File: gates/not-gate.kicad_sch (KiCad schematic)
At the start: 5 parts, among them Q7 NPN, Q8 NPN

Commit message: Schematic for register
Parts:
- removed Q7, Q8: NPN, symbol Simulation_SPICE:NPN
- removed R12, R13: 10k, Resistor_SMD:R_0201_0603Metric, symbol Device:R
- removed R14: 4.7k, Resistor_SMD:R_0201_0603Metric, symbol Device:R
- added Q1: NPN, symbol Simulation_SPICE:NPN
- added R1: 10k, symbol Device:R
- added R2: 4.7k, symbol Device:R
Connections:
- net +5V: now also R2.2
- net A: now also R1.1
- net GND: now also Q1.3 (E)
- net OUTPUT: now also Q1.1 (C), R2.1
- new net: Q1.2 (B), R1.2

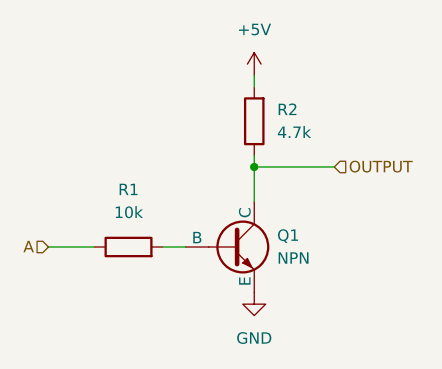
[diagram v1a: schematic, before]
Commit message: Schematic of control-unit
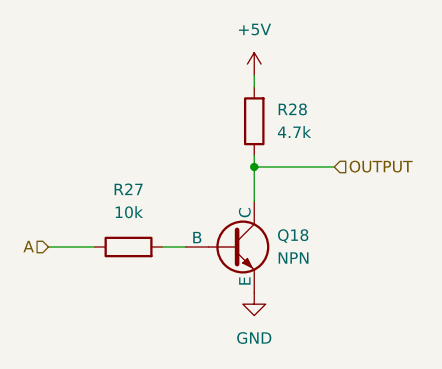
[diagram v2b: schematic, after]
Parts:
- renumbered Q1 to Q18, R1 to R27, R2 to R28
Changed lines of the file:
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@@
 		(dnp no)
 		(fields_autoplaced yes)
-		(property "Reference" "#PWR05"
+		(property "Reference" "#PWR027"
 			(at 87.63 55.88 0)
 			(effects
@@
 		)
 		(instances
-			(project "register"
-				(path "/176ebc34-d92d-46b0-a9f1-4fb76aa55196/1641c1b9-e3d9-452a-a206-0a4a18cb7a68/6e38e628-9b38-49db-b4e0-13318949e362"
-					(reference "#PWR019")
-					(unit 1)
-				)
-				(path "/176ebc34-d92d-46b0-a9f1-4fb76aa55196/2b210005-c9ef-43dd-bd20-4304cf65b93c/6e38e628-9b38-49db-b4e0-13318949e362"
-					(reference "#PWR05")
-					(unit 1)
-				)
-				(path "/176ebc34-d92d-46b0-a9f1-4fb76aa55196/475a755d-c11d-42bc-b5a5-c2bbb617acf6/6e38e628-9b38-49db-b4e0-13318949e362"
-					(reference "#PWR047")
-					(unit 1)
-				)
-				(path "/176ebc34-d92d-46b0-a9f1-4fb76aa55196/510c109f-9f77-4fcd-9065-7421496291db/6e38e628-9b38-49db-b4e0-13318949e362"
-					(reference "#PWR033")
+			(project "control-unit"
+				(path "/1cf3a7ee-ec47-45b6-b515-1840d726ab8f/020249bf-5e28-4526-a135-e7e504fcd315"
+					(reference "#PWR?")
+					(unit 1)
+				)
+				(path "/1cf3a7ee-ec47-45b6-b515-1840d726ab8f/0384bfed-f155-4b67-acfd-5caa02b59c9d"
+					(reference "#PWR027")
+					(unit 1)
+				)
+				(path "/1cf3a7ee-ec47-45b6-b515-1840d726ab8f/32697942-fb33-4fba-8e0d-2ff095b080bf"
+					(reference "#PWR017")
+					(unit 1)
+				)
+				(path "/1cf3a7ee-ec47-45b6-b515-1840d726ab8f/80b2507e-0011-4117-8a6b-d09ffa023d4d"
+					(reference "#PWR039")
+					(unit 1)
+				)
+				(path "/1cf3a7ee-ec47-45b6-b515-1840d726ab8f/b2ec3573-bf15-4e1d-8a02-9a033baafe0c"
+					(reference "#PWR021")
+					(unit 1)
+				)
+				(path "/1cf3a7ee-ec47-45b6-b515-1840d726ab8f/b421555f-23f8-4bc1-97f9-21732f6fe247"
+					(reference "#PWR025")
 					(unit 1)
 				)
@@
 		(dnp no)
 		(fields_autoplaced yes)
-		(property "Reference" "R1"
+		(property "Reference" "R27"
 			(at 73.66 64.77 90)
 			(effects
@@
 		)
 		(instances
-			(project "register"
-				(path "/176ebc34-d92d-46b0-a9f1-4fb76aa55196/1641c1b9-e3d9-452a-a206-0a4a18cb7a68/6e38e628-9b38-49db-b4e0-13318949e362"
+			(project "control-unit"
+				(path "/1cf3a7ee-ec47-45b6-b515-1840d726ab8f/020249bf-5e28-4526-a135-e7e504fcd315"
+					(reference "R?")
+					(unit 1)
+				)
+				(path "/1cf3a7ee-ec47-45b6-b515-1840d726ab8f/0384bfed-f155-4b67-acfd-5caa02b59c9d"
+					(reference "R27")
+					(unit 1)
+				)
+				(path "/1cf3a7ee-ec47-45b6-b515-1840d726ab8f/32697942-fb33-4fba-8e0d-2ff095b080bf"
+					(reference "R23")
+					(unit 1)
+				)
+				(path "/1cf3a7ee-ec47-45b6-b515-1840d726ab8f/80b2507e-0011-4117-8a6b-d09ffa023d4d"
+					(reference "R37")
+					(unit 1)
+				)
+				(path "/1cf3a7ee-ec47-45b6-b515-1840d726ab8f/b2ec3573-bf15-4e1d-8a02-9a033baafe0c"
 					(reference "R17")
 					(unit 1)
 				)
-				(path "/176ebc34-d92d-46b0-a9f1-4fb76aa55196/2b210005-c9ef-43dd-bd20-4304cf65b93c/6e38e628-9b38-49db-b4e0-13318949e362"
-					(reference "R1")
-					(unit 1)
-				)
-				(path "/176ebc34-d92d-46b0-a9f1-4fb76aa55196/475a755d-c11d-42bc-b5a5-c2bbb617acf6/6e38e628-9b38-49db-b4e0-13318949e362"
-					(reference "R49")
-					(unit 1)
-				)
-				(path "/176ebc34-d92d-46b0-a9f1-4fb76aa55196/510c109f-9f77-4fcd-9065-7421496291db/6e38e628-9b38-49db-b4e0-13318949e362"
-					(reference "R33")
+				(path "/1cf3a7ee-ec47-45b6-b515-1840d726ab8f/b421555f-23f8-4bc1-97f9-21732f6fe247"
+					(reference "R25")
 					(unit 1)
 				)
@@
 		(dnp no)
 		(fields_autoplaced yes)
-		(property "Reference" "R2"
+		(property "Reference" "R28"
 			(at 90.17 55.8799 0)
 			(effects
@@
 		)
 		(instances
-			(project "register"
-				(path "/176ebc34-d92d-46b0-a9f1-4fb76aa55196/1641c1b9-e3d9-452a-a206-0a4a18cb7a68/6e38e628-9b38-49db-b4e0-13318949e362"
+			(project "control-unit"
+				(path "/1cf3a7ee-ec47-45b6-b515-1840d726ab8f/020249bf-5e28-4526-a135-e7e504fcd315"
+					(reference "R?")
+					(unit 1)
+				)
+				(path "/1cf3a7ee-ec47-45b6-b515-1840d726ab8f/0384bfed-f155-4b67-acfd-5caa02b59c9d"
+					(reference "R28")
+					(unit 1)
+				)
+				(path "/1cf3a7ee-ec47-45b6-b515-1840d726ab8f/32697942-fb33-4fba-8e0d-2ff095b080bf"
+					(reference "R24")
+					(unit 1)
+				)
+				(path "/1cf3a7ee-ec47-45b6-b515-1840d726ab8f/80b2507e-0011-4117-8a6b-d09ffa023d4d"
+					(reference "R38")
+					(unit 1)
+				)
+				(path "/1cf3a7ee-ec47-45b6-b515-1840d726ab8f/b2ec3573-bf15-4e1d-8a02-9a033baafe0c"
 					(reference "R18")
 					(unit 1)
 				)
-				(path "/176ebc34-d92d-46b0-a9f1-4fb76aa55196/2b210005-c9ef-43dd-bd20-4304cf65b93c/6e38e628-9b38-49db-b4e0-13318949e362"
-					(reference "R2")
-					(unit 1)
-				)
-				(path "/176ebc34-d92d-46b0-a9f1-4fb76aa55196/475a755d-c11d-42bc-b5a5-c2bbb617acf6/6e38e628-9b38-49db-b4e0-13318949e362"
-					(reference "R50")
-					(unit 1)
-				)
-				(path "/176ebc34-d92d-46b0-a9f1-4fb76aa55196/510c109f-9f77-4fcd-9065-7421496291db/6e38e628-9b38-49db-b4e0-13318949e362"
-					(reference "R34")
+				(path "/1cf3a7ee-ec47-45b6-b515-1840d726ab8f/b421555f-23f8-4bc1-97f9-21732f6fe247"
+					(reference "R26")
 					(unit 1)
 				)
@@
 		(dnp no)
 		(fields_autoplaced yes)
-		(property "Reference" "#PWR06"
+		(property "Reference" "#PWR028"
 			(at 87.63 82.55 0)
 			(effects
@@
 		)
 		(instances
-			(project "register"
-				(path "/176ebc34-d92d-46b0-a9f1-4fb76aa55196/1641c1b9-e3d9-452a-a206-0a4a18cb7a68/6e38e628-9b38-49db-b4e0-13318949e362"
-					(reference "#PWR020")
-					(unit 1)
-				)
-				(path "/176ebc34-d92d-46b0-a9f1-4fb76aa55196/2b210005-c9ef-43dd-bd20-4304cf65b93c/6e38e628-9b38-49db-b4e0-13318949e362"
-					(reference "#PWR06")
-					(unit 1)
-				)
-				(path "/176ebc34-d92d-46b0-a9f1-4fb76aa55196/475a755d-c11d-42bc-b5a5-c2bbb617acf6/6e38e628-9b38-49db-b4e0-13318949e362"
-					(reference "#PWR048")
-					(unit 1)
-				)
-				(path "/176ebc34-d92d-46b0-a9f1-4fb76aa55196/510c109f-9f77-4fcd-9065-7421496291db/6e38e628-9b38-49db-b4e0-13318949e362"
-					(reference "#PWR034")
+			(project "control-unit"
+				(path "/1cf3a7ee-ec47-45b6-b515-1840d726ab8f/020249bf-5e28-4526-a135-e7e504fcd315"
+					(reference "#PWR?")
+					(unit 1)
+				)
+				(path "/1cf3a7ee-ec47-45b6-b515-1840d726ab8f/0384bfed-f155-4b67-acfd-5caa02b59c9d"
+					(reference "#PWR028")
+					(unit 1)
+				)
+				(path "/1cf3a7ee-ec47-45b6-b515-1840d726ab8f/32697942-fb33-4fba-8e0d-2ff095b080bf"
+					(reference "#PWR018")
+					(unit 1)
+				)
+				(path "/1cf3a7ee-ec47-45b6-b515-1840d726ab8f/80b2507e-0011-4117-8a6b-d09ffa023d4d"
+					(reference "#PWR040")
+					(unit 1)
+				)
+				(path "/1cf3a7ee-ec47-45b6-b515-1840d726ab8f/b2ec3573-bf15-4e1d-8a02-9a033baafe0c"
+					(reference "#PWR022")
+					(unit 1)
+				)
+				(path "/1cf3a7ee-ec47-45b6-b515-1840d726ab8f/b421555f-23f8-4bc1-97f9-21732f6fe247"
+					(reference "#PWR026")
 					(unit 1)
 				)
@@
 		(dnp no)
 		(fields_autoplaced yes)
-		(property "Reference" "Q1"
+		(property "Reference" "Q18"
 			(at 90.17 69.8499 0)
 			(effects
@@
 		)
 		(instances
-			(project "register"
-				(path "/176ebc34-d92d-46b0-a9f1-4fb76aa55196/1641c1b9-e3d9-452a-a206-0a4a18cb7a68/6e38e628-9b38-49db-b4e0-13318949e362"
-					(reference "Q12")
-					(unit 1)
-				)
-				(path "/176ebc34-d92d-46b0-a9f1-4fb76aa55196/2b210005-c9ef-43dd-bd20-4304cf65b93c/6e38e628-9b38-49db-b4e0-13318949e362"
-					(reference "Q1")
-					(unit 1)
-				)
-				(path "/176ebc34-d92d-46b0-a9f1-4fb76aa55196/475a755d-c11d-42bc-b5a5-c2bbb617acf6/6e38e628-9b38-49db-b4e0-13318949e362"
-					(reference "Q34")
-					(unit 1)
-				)
-				(path "/176ebc34-d92d-46b0-a9f1-4fb76aa55196/510c109f-9f77-4fcd-9065-7421496291db/6e38e628-9b38-49db-b4e0-13318949e362"
-					(reference "Q23")
-					(unit 1)
-				)
+			(project "control-unit"
+				(path "/1cf3a7ee-ec47-45b6-b515-1840d726ab8f/020249bf-5e28-4526-a135-e7e504fcd315"
+					(reference "Q?")
+					(unit 1)
+				)
+				(path "/1cf3a7ee-ec47-45b6-b515-1840d726ab8f/0384bfed-f155-4b67-acfd-5caa02b59c9d"
+					(reference "Q18")
+					(unit 1)
+				)
+				(path "/1cf3a7ee-ec47-45b6-b515-1840d726ab8f/32697942-fb33-4fba-8e0d-2ff095b080bf"
+					(reference "Q16")
+					(unit 1)
+				)
+				(path "/1cf3a7ee-ec47-45b6-b515-1840d726ab8f/80b2507e-0011-4117-8a6b-d09ffa023d4d"
+					(reference "Q26")
+					(unit 1)
+				)
+				(path "/1cf3a7ee-ec47-45b6-b515-1840d726ab8f/b2ec3573-bf15-4e1d-8a02-9a033baafe0c"
+					(reference "Q13")
+					(unit 1)
+				)
+				(path "/1cf3a7ee-ec47-45b6-b515-1840d726ab8f/b421555f-23f8-4bc1-97f9-21732f6fe247"
+					(reference "Q17")
+					(unit 1)
+				)

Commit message: Alternative and gates with different amounts of inputs
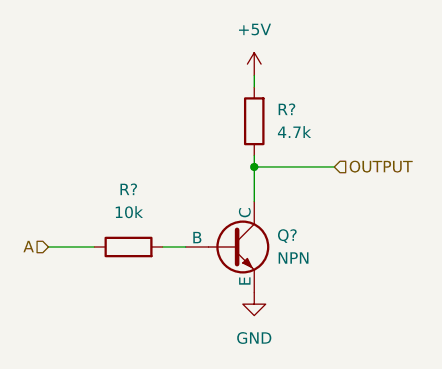
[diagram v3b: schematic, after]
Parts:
- renumbered Q18 to Q?, R27 to R?, R28 to R?
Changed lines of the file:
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@@
 		(dnp no)
 		(fields_autoplaced yes)
-		(property "Reference" "#PWR027"
+		(property "Reference" "#PWR?"
 			(at 87.63 55.88 0)
 			(effects
@@
 		(dnp no)
 		(fields_autoplaced yes)
-		(property "Reference" "R27"
+		(property "Reference" "R?"
 			(at 73.66 64.77 90)
 			(effects
@@
 		(dnp no)
 		(fields_autoplaced yes)
-		(property "Reference" "R28"
+		(property "Reference" "R?"
 			(at 90.17 55.8799 0)
 			(effects
@@
 		(dnp no)
 		(fields_autoplaced yes)
-		(property "Reference" "#PWR028"
+		(property "Reference" "#PWR?"
 			(at 87.63 82.55 0)
 			(effects
@@
 		(dnp no)
 		(fields_autoplaced yes)
-		(property "Reference" "Q18"
+		(property "Reference" "Q?"
 			(at 90.17 69.8499 0)
 			(effects

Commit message: complete 2-bit encoder
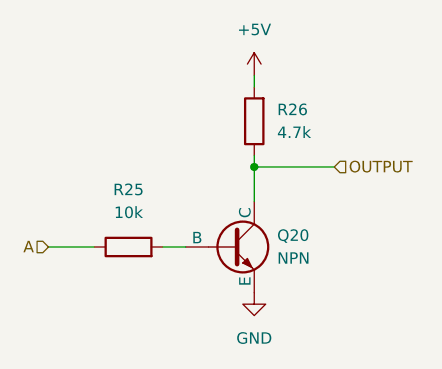
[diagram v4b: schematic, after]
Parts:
- gave numbers to parts that had none: 3
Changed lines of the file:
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@@
 		(dnp no)
 		(fields_autoplaced yes)
-		(property "Reference" "#PWR?"
+		(property "Reference" "#PWR025"
 			(at 87.63 55.88 0)
 			(effects
@@
 			(project "control-unit"
 				(path "/1cf3a7ee-ec47-45b6-b515-1840d726ab8f/020249bf-5e28-4526-a135-e7e504fcd315"
-					(reference "#PWR?")
+					(reference "#PWR025")
 					(unit 1)
 				)
 				(path "/1cf3a7ee-ec47-45b6-b515-1840d726ab8f/0384bfed-f155-4b67-acfd-5caa02b59c9d"
+					(reference "#PWR031")
+					(unit 1)
+				)
+				(path "/1cf3a7ee-ec47-45b6-b515-1840d726ab8f/32697942-fb33-4fba-8e0d-2ff095b080bf"
 					(reference "#PWR027")
 					(unit 1)
 				)
-				(path "/1cf3a7ee-ec47-45b6-b515-1840d726ab8f/32697942-fb33-4fba-8e0d-2ff095b080bf"
-					(reference "#PWR017")
-					(unit 1)
-				)
 				(path "/1cf3a7ee-ec47-45b6-b515-1840d726ab8f/80b2507e-0011-4117-8a6b-d09ffa023d4d"
-					(reference "#PWR039")
+					(reference "#PWR098")
 					(unit 1)
 				)
 				(path "/1cf3a7ee-ec47-45b6-b515-1840d726ab8f/b2ec3573-bf15-4e1d-8a02-9a033baafe0c"
-					(reference "#PWR021")
+					(reference "#PWR088")
 					(unit 1)
 				)
 				(path "/1cf3a7ee-ec47-45b6-b515-1840d726ab8f/b421555f-23f8-4bc1-97f9-21732f6fe247"
-					(reference "#PWR025")
+					(reference "#PWR029")
+					(unit 1)
+				)
+				(path "/1cf3a7ee-ec47-45b6-b515-1840d726ab8f/3b093a12-0540-43ca-8877-b58e062186b8/77964015-ec89-42e0-893c-6358bdc5e5f2"
+					(reference "#PWR0118")
+					(unit 1)
+				)
+				(path "/1cf3a7ee-ec47-45b6-b515-1840d726ab8f/3b093a12-0540-43ca-8877-b58e062186b8/c4e913ae-1921-4602-80cf-8d8d9fdbe077"
+					(reference "#PWR0116")
 					(unit 1)
 				)
@@
 		(dnp no)
 		(fields_autoplaced yes)
-		(property "Reference" "R?"
+		(property "Reference" "R25"
 			(at 73.66 64.77 90)
 			(effects
@@
 			(project "control-unit"
 				(path "/1cf3a7ee-ec47-45b6-b515-1840d726ab8f/020249bf-5e28-4526-a135-e7e504fcd315"
-					(reference "R?")
+					(reference "R25")
 					(unit 1)
 				)
 				(path "/1cf3a7ee-ec47-45b6-b515-1840d726ab8f/0384bfed-f155-4b67-acfd-5caa02b59c9d"
+					(reference "R31")
+					(unit 1)
+				)
+				(path "/1cf3a7ee-ec47-45b6-b515-1840d726ab8f/32697942-fb33-4fba-8e0d-2ff095b080bf"
 					(reference "R27")
 					(unit 1)
 				)
-				(path "/1cf3a7ee-ec47-45b6-b515-1840d726ab8f/32697942-fb33-4fba-8e0d-2ff095b080bf"
-					(reference "R23")
-					(unit 1)
-				)
 				(path "/1cf3a7ee-ec47-45b6-b515-1840d726ab8f/80b2507e-0011-4117-8a6b-d09ffa023d4d"
-					(reference "R37")
+					(reference "R108")
 					(unit 1)
 				)
 				(path "/1cf3a7ee-ec47-45b6-b515-1840d726ab8f/b2ec3573-bf15-4e1d-8a02-9a033baafe0c"
-					(reference "R17")
+					(reference "R98")
 					(unit 1)
 				)
 				(path "/1cf3a7ee-ec47-45b6-b515-1840d726ab8f/b421555f-23f8-4bc1-97f9-21732f6fe247"
-					(reference "R25")
+					(reference "R29")
+					(unit 1)
+				)
+				(path "/1cf3a7ee-ec47-45b6-b515-1840d726ab8f/3b093a12-0540-43ca-8877-b58e062186b8/77964015-ec89-42e0-893c-6358bdc5e5f2"
+					(reference "R128")
+					(unit 1)
+				)
+				(path "/1cf3a7ee-ec47-45b6-b515-1840d726ab8f/3b093a12-0540-43ca-8877-b58e062186b8/c4e913ae-1921-4602-80cf-8d8d9fdbe077"
+					(reference "R126")
 					(unit 1)
 				)
@@
 		(dnp no)
 		(fields_autoplaced yes)
-		(property "Reference" "R?"
+		(property "Reference" "R26"
 			(at 90.17 55.8799 0)
 			(effects
@@
 			(project "control-unit"
 				(path "/1cf3a7ee-ec47-45b6-b515-1840d726ab8f/020249bf-5e28-4526-a135-e7e504fcd315"
-					(reference "R?")
+					(reference "R26")
 					(unit 1)
 				)
 				(path "/1cf3a7ee-ec47-45b6-b515-1840d726ab8f/0384bfed-f155-4b67-acfd-5caa02b59c9d"
+					(reference "R32")
+					(unit 1)
+				)
+				(path "/1cf3a7ee-ec47-45b6-b515-1840d726ab8f/32697942-fb33-4fba-8e0d-2ff095b080bf"
 					(reference "R28")
 					(unit 1)
 				)
-				(path "/1cf3a7ee-ec47-45b6-b515-1840d726ab8f/32697942-fb33-4fba-8e0d-2ff095b080bf"
-					(reference "R24")
-					(unit 1)
-				)
 				(path "/1cf3a7ee-ec47-45b6-b515-1840d726ab8f/80b2507e-0011-4117-8a6b-d09ffa023d4d"
-					(reference "R38")
+					(reference "R109")
 					(unit 1)
 				)
 				(path "/1cf3a7ee-ec47-45b6-b515-1840d726ab8f/b2ec3573-bf15-4e1d-8a02-9a033baafe0c"
-					(reference "R18")
+					(reference "R99")
 					(unit 1)
 				)
 				(path "/1cf3a7ee-ec47-45b6-b515-1840d726ab8f/b421555f-23f8-4bc1-97f9-21732f6fe247"
-					(reference "R26")
+					(reference "R30")
+					(unit 1)
+				)
+				(path "/1cf3a7ee-ec47-45b6-b515-1840d726ab8f/3b093a12-0540-43ca-8877-b58e062186b8/77964015-ec89-42e0-893c-6358bdc5e5f2"
+					(reference "R129")
+					(unit 1)
+				)
+				(path "/1cf3a7ee-ec47-45b6-b515-1840d726ab8f/3b093a12-0540-43ca-8877-b58e062186b8/c4e913ae-1921-4602-80cf-8d8d9fdbe077"
+					(reference "R127")
 					(unit 1)
 				)
@@
 		(dnp no)
 		(fields_autoplaced yes)
-		(property "Reference" "#PWR?"
+		(property "Reference" "#PWR026"
 			(at 87.63 82.55 0)
 			(effects
@@
 			(project "control-unit"
 				(path "/1cf3a7ee-ec47-45b6-b515-1840d726ab8f/020249bf-5e28-4526-a135-e7e504fcd315"
-					(reference "#PWR?")
+					(reference "#PWR026")
 					(unit 1)
 				)
 				(path "/1cf3a7ee-ec47-45b6-b515-1840d726ab8f/0384bfed-f155-4b67-acfd-5caa02b59c9d"
+					(reference "#PWR032")
+					(unit 1)
+				)
+				(path "/1cf3a7ee-ec47-45b6-b515-1840d726ab8f/32697942-fb33-4fba-8e0d-2ff095b080bf"
 					(reference "#PWR028")
 					(unit 1)
 				)
-				(path "/1cf3a7ee-ec47-45b6-b515-1840d726ab8f/32697942-fb33-4fba-8e0d-2ff095b080bf"
-					(reference "#PWR018")
-					(unit 1)
-				)
 				(path "/1cf3a7ee-ec47-45b6-b515-1840d726ab8f/80b2507e-0011-4117-8a6b-d09ffa023d4d"
-					(reference "#PWR040")
+					(reference "#PWR099")
 					(unit 1)
 				)
 				(path "/1cf3a7ee-ec47-45b6-b515-1840d726ab8f/b2ec3573-bf15-4e1d-8a02-9a033baafe0c"
-					(reference "#PWR022")
+					(reference "#PWR089")
 					(unit 1)
 				)
 				(path "/1cf3a7ee-ec47-45b6-b515-1840d726ab8f/b421555f-23f8-4bc1-97f9-21732f6fe247"
-					(reference "#PWR026")
+					(reference "#PWR030")
+					(unit 1)
+				)
+				(path "/1cf3a7ee-ec47-45b6-b515-1840d726ab8f/3b093a12-0540-43ca-8877-b58e062186b8/77964015-ec89-42e0-893c-6358bdc5e5f2"
+					(reference "#PWR0119")
+					(unit 1)
+				)
+				(path "/1cf3a7ee-ec47-45b6-b515-1840d726ab8f/3b093a12-0540-43ca-8877-b58e062186b8/c4e913ae-1921-4602-80cf-8d8d9fdbe077"
+					(reference "#PWR0117")
 					(unit 1)
 				)
@@
 		(dnp no)
 		(fields_autoplaced yes)
-		(property "Reference" "Q?"
+		(property "Reference" "Q20"
 			(at 90.17 69.8499 0)
 			(effects
@@
 			(project "control-unit"
 				(path "/1cf3a7ee-ec47-45b6-b515-1840d726ab8f/020249bf-5e28-4526-a135-e7e504fcd315"
-					(reference "Q?")
+					(reference "Q20")
 					(unit 1)
 				)
 				(path "/1cf3a7ee-ec47-45b6-b515-1840d726ab8f/0384bfed-f155-4b67-acfd-5caa02b59c9d"
-					(reference "Q18")
+					(reference "Q23")
 					(unit 1)
 				)
 				(path "/1cf3a7ee-ec47-45b6-b515-1840d726ab8f/32697942-fb33-4fba-8e0d-2ff095b080bf"
-					(reference "Q16")
+					(reference "Q21")
 					(unit 1)
 				)
 				(path "/1cf3a7ee-ec47-45b6-b515-1840d726ab8f/80b2507e-0011-4117-8a6b-d09ffa023d4d"
-					(reference "Q26")
+					(reference "Q83")
 					(unit 1)
 				)
 				(path "/1cf3a7ee-ec47-45b6-b515-1840d726ab8f/b2ec3573-bf15-4e1d-8a02-9a033baafe0c"
-					(reference "Q13")
+					(reference "Q76")
 					(unit 1)
 				)
 				(path "/1cf3a7ee-ec47-45b6-b515-1840d726ab8f/b421555f-23f8-4bc1-97f9-21732f6fe247"
-					(reference "Q17")
-					(unit 1)
-				)
+					(reference "Q22")
+					(unit 1)
+				)
+				(path "/1cf3a7ee-ec47-45b6-b515-1840d726ab8f/3b093a12-0540-43ca-8877-b58e062186b8/77964015-ec89-42e0-893c-6358bdc5e5f2"
+					(reference "Q97")
+					(unit 1)
+				)
+				(path "/1cf3a7ee-ec47-45b6-b515-1840d726ab8f/3b093a12-0540-43ca-8877-b58e062186b8/c4e913ae-1921-4602-80cf-8d8d9fdbe077"
+					(reference "Q96")
+					(unit 1)
+				)
